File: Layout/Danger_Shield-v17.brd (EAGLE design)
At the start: 80 x 105.4 mm, 35 parts, among them U1 ARDUINO_SHIELDNO_SILK, U2 74LS595N, U3 LM335

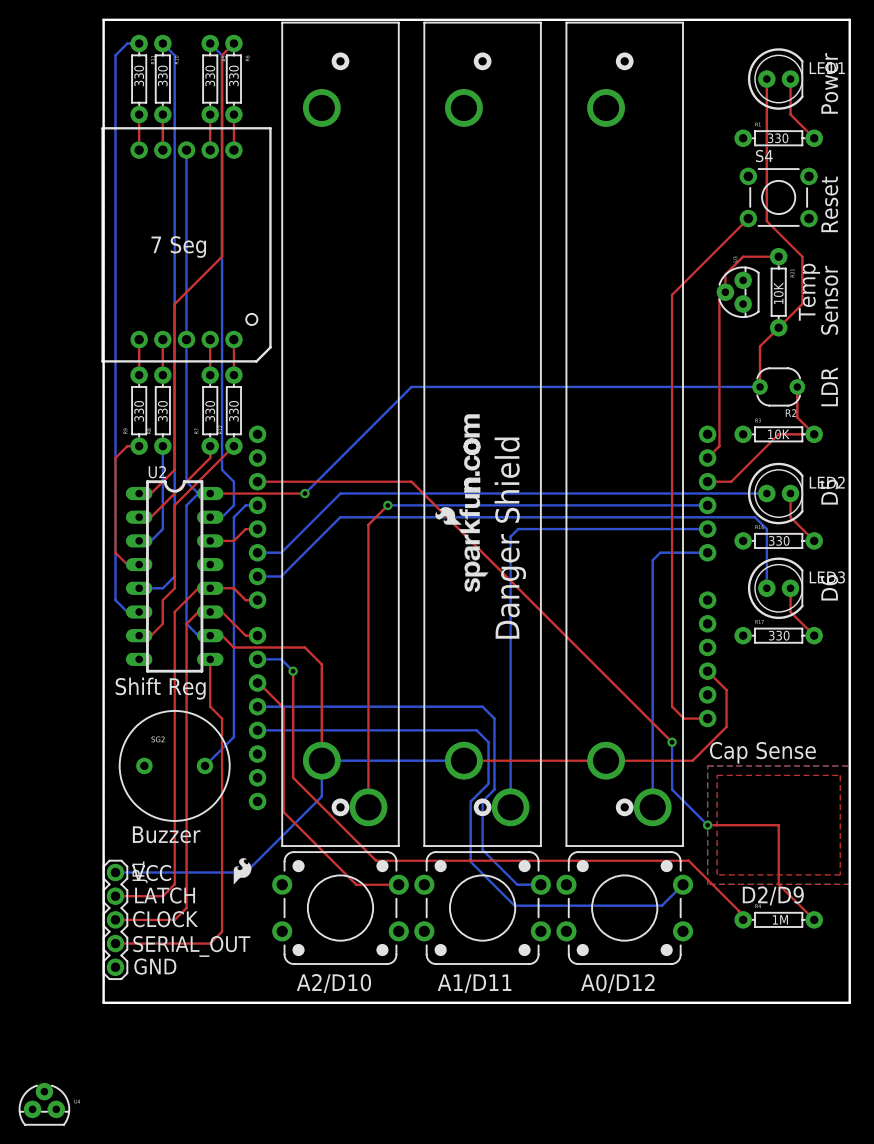
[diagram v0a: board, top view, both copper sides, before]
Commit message: v1.7 changes temp sensor to TMP36. Add 2 caps.
Removed 10k on temp sensor. Changed to TMP36. Added 2 x 0.1uF caps for
decoupling on shift register and temp sensor.
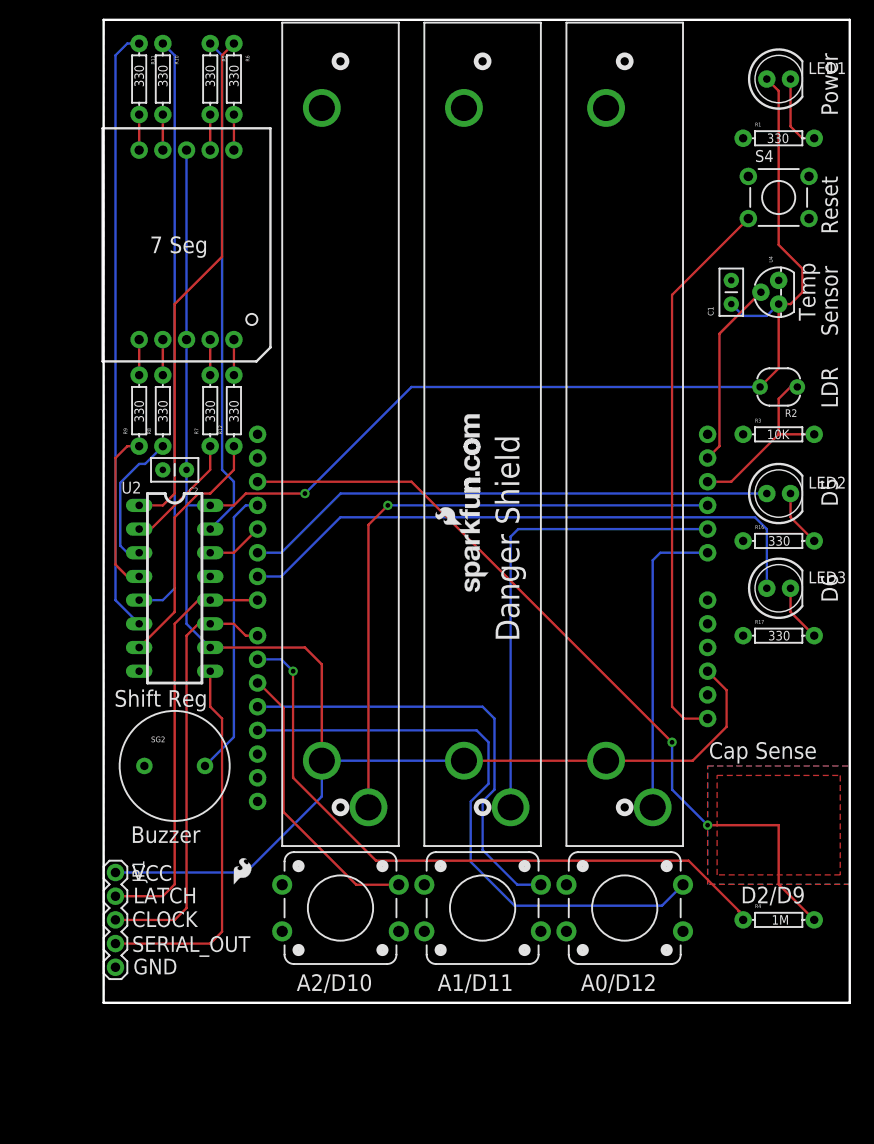
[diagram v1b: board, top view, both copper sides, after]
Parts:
- removed R21: 10K, SparkFun:AXIAL-0.3
- removed U3: LM335, SparkFun:TO-92
- added C1, C2: 0.1uF, SparkFun-Passives:CAP-PTH-SMALL2
- U4: value (none) -> TMP36
- moved U4 117.8 mm to (72.4, 76.2), turned to 90 degrees
- moved U2 1.27 mm to (7.62, 44.5)
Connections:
- net A4: now also U4.2; no longer R21.P$1, U3.2
- net GND: now also C1.2, C2.2, U4.3; no longer U3.3
- net VCC: now also C1.1, C2.1, U4.1; no longer R21.P$2
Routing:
- net VCC: track 261.0 -> 268.6 mm
- net A4: track 27.0 -> 20.1 mm
- net N$6: track 12.0 -> 15.3 mm
- net N$4: track 53.2 -> 55.2 mm
- net LATCH: track 46.6 -> 44.8 mm
- net CLOCK: track 47.8 -> 46.0 mm
- net N$8: track 62.0 -> 63.3 mm
- net N$5: track 11.5 -> 12.8 mm
- net N$7: track 16.3 -> 17.6 mm
- net SERIAL_OUT: track 41.7 -> 40.4 mm
- net N$10: track 25.3 -> 26.5 mm
- net N$3: track 7.40 -> 8.15 mm
- net SERIAL_IN: track 5.61 -> 6.13 mm
- net N$9: track 64.6 -> 65.1 mm
- net N$2: track 53.6 -> 54.2 mm
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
